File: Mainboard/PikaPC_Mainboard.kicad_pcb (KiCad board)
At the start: 2 copper layers, 190.5 x 147.3 mm, 87 parts, among them J1 Conn_02x08_Odd_Even, J10 Conn_01x08, J11 Conn_01x08, J12 Conn_01x08, J13 Conn_01x08, J14 Conn_01x08, J15 Conn_01x08, J16 Conn_01x08, J17 Conn_01x08, J18 Conn_01x10, J19 Conn_02x05_Odd_Even, J5 DIN41612_03x32_C_Split, J6 Mini-DIN-6, J7 Mini-DIN-6, J9 Conn_01x08, SW1 SW_Push_DPDT, SW2 SW_Push, U1 PPC403GA, U10 74LS07, U11 86C325, U12 GD75232N, U13 74LVC125, U14 MCP120-315GI/TO, U15 AS6C4008-55PCN, U16 AS6C4008-55PCN, U17 ATF1504, U18 T224162B, U19 T224162B, U2 SN74LVC245A, U20 T224162B, U21 T224162B, U22 SN74LVC245A, U23 SN74LVC245A, U3 SST39VF010, U4 SN74LVC245A, U5 SN74LVC245A, U6 SN74LVC245A, U7 8042 PS/2, U8 SN74LVC245A, U9 74LS04, Y1 25M, Y2 7M3728, Y3 14M31818

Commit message: VRAM control debugging
- correct clock edge for VLB ReadyIn
- minor tweaks for S3 ViRGE symbol
- add series resistors to VRAM control signals
- add strapping resistor to support Trio64V+
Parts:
- added RN10: 33R, Resistor_THT:R_Array_SIP10, F.Cu at (195.6, 27.9)
- added RN11: 33R, Resistor_THT:R_Array_SIP10, F.Cu at (205.7, 43.2)
- added RN12: 33R, Resistor_THT:R_Array_SIP10, F.Cu at (205.7, 71.1)
- added RN9: 10X-1-472LF, Resistor_THT:R_Array_SIP10, F.Cu at (195.6, 33.0)
- moved C24 52.3 mm to (149.9, 45.7), turned to 0 degrees
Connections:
- RN5 pad 2: unconnected-(RN5-R1-Pad2) -> /VID-SAUP2
- RN6 pad 7: unconnected-(RN6-R6-Pad7) -> /VMD24
- U11 pad 148: unconnected-(U11D-LCLK-Pad148) -> /VLCLK
- U11 pad 203: unconnected-(U11D-~{VREQ}-Pad203) -> /VEVIDEO
- U11 pad 204: unconnected-(U11D-~{CREQ}-Pad204) -> /~{VCREQ}
- U11 pad 205: unconnected-(U11D-SPCLK-Pad205) -> /VESYNC
- U11 pad 206: unconnected-(U11D-SPD-Pad206) -> /~{VBLANK}
- U18 pad 13: /~{VMWE} -> /~{VMWER}
- U18 pad 14: /~{VMRAS0} -> /~{VMRAS0R}
- U18 pad 27: /~{VMOE} -> /~{VMOER}
- U19 pad 13: /~{VMWE} -> /~{VMWER}
- U19 pad 14: /~{VMRAS0} -> /~{VMRAS0R}
- U19 pad 27: /~{VMOE} -> /~{VMOER}
- U20 pad 13: /~{VMWE} -> /~{VMWER}
- U20 pad 14: /~{VMRAS0} -> /~{VMRAS0R}
- U20 pad 27: /~{VMOE} -> /~{VMOER}
- U21 pad 13: /~{VMWE} -> /~{VMWER}
- U21 pad 14: /~{VMRAS0} -> /~{VMRAS0R}
- U21 pad 27: /~{VMOE} -> /~{VMOER}
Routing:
- net /~{VMRAS0}: track 37.9 -> 8.86 mm
- net /~{VMRAS0R}: track 0.00 -> 29.1 mm
- net /~{VMOER}: track 0.00 -> 29.1 mm
- net /~{VMOE}: track 37.7 -> 8.66 mm
- net unconnected-(U11D-SPCLK-Pad205): track 18.4 -> 0.00 mm
- net /VESYNC: track 0.00 -> 18.4 mm
- net /~{VMWE}: track 28.2 -> 11.4 mm
- net /~{VMWER}: track 0.00 -> 16.8 mm
- net unconnected-(U11D-~{CREQ}-Pad204): track 15.8 -> 0.00 mm
- net /~{VCREQ}: track 0.00 -> 15.8 mm
- net unconnected-(U11D-SPD-Pad206): track 13.1 -> 0.00 mm
- net /~{VBLANK}: track 0.00 -> 13.1 mm
- net unconnected-(U11D-~{VREQ}-Pad203): track 11.8 -> 0.00 mm
- net /VEVIDEO: track 0.00 -> 11.8 mm
- net unconnected-(U11D-LCLK-Pad148): track 10.6 -> 0.00 mm
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
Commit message: Add new bus to wire-wrap mainboard
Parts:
- removed C19, C20, C21, C22: 47p, Capacitor_THT:C_Disc_D3.0mm_W2.0mm_P2.50mm
- removed C23, C24: 100nF, Capacitor_THT:C_Disc_D3.0mm_W2.0mm_P2.50mm
- removed FB1, FB2, FB3: FerriteBead, Inductor_THT:L_Axial_L7.0mm_D3.3mm_P5.08mm_Vertical_Fastron_MICC
- removed J1: Conn_02x08_Odd_Even, Connector_PinHeader_2.54mm:PinHeader_2x08_P2.54mm_Vertical
- removed J6, J7: Mini-DIN-6, Connector_PinHeader_2.54mm:PinHeader_2x03_P2.54mm_Vertical
- removed R11, R6, R7: 75R, Resistor_THT:R_Axial_DIN0204_L3.6mm_D1.6mm_P2.54mm_Vertical
- removed R2: 220R, Resistor_THT:R_Axial_DIN0204_L3.6mm_D1.6mm_P2.54mm_Vertical
- removed R3: 470R, Resistor_THT:R_Axial_DIN0204_L3.6mm_D1.6mm_P2.54mm_Vertical
- removed RN10, RN11, RN12: 33R, Resistor_THT:R_Array_SIP10
- removed RN4, RN6, RN8: 9A103J, Resistor_THT:R_Array_SIP9
- removed RN7: 10X-1-472F, Resistor_THT:R_Array_SIP9
- removed RN9: 10X-1-472LF, Resistor_THT:R_Array_SIP10
- removed U11: 86C325, Package_QFP:PQFP-208_28x28mm_P0.5mm
- removed U17: ATF1504, Package_LCC:PLCC-44_THT-Socket
- removed U18, U19, U20, U21: T224162B, Package_SO:SOJ-44_10.16x28.575mm_P1.27mm
- removed U22, U23, U4, U5, U6, U8: SN74LVC245A, Package_DIP:DIP-20_W7.62mm_Socket
- removed U7: 8042 PS/2, Package_DIP:DIP-40_W15.24mm_Socket
- removed Y3: 14M31818, Oscillator:Oscillator_DIP-8
- added U101: SN74LVC245A, Package_DIP:DIP-20_W7.62mm_Socket, F.Cu at (104.1, 78.7)
- added U102: SN74LVC245A, Package_DIP:DIP-20_W7.62mm_Socket, F.Cu at (132.1, 78.7)
- added U103: SN74LVC245A, Package_DIP:DIP-20_W7.62mm_Socket, F.Cu at (104.1, 66.0)
- added U104: SN74LVC245A, Package_DIP:DIP-20_W7.62mm_Socket, F.Cu at (132.1, 66.0)
- added U105: SN74LVC245A, Package_DIP:DIP-20_W7.62mm_Socket, F.Cu at (132.1, 53.3)
- added U106: SN74LVC245A, Package_DIP:DIP-20_W7.62mm_Socket, F.Cu at (104.1, 53.3)
- added U107: SN74LVC245A, Package_DIP:DIP-20_W7.62mm_Socket, F.Cu at (104.1, 40.6)
- added U108: SN74LVC245A, Package_DIP:DIP-20_W7.62mm_Socket, F.Cu at (132.1, 40.6)
- added U109: 74LS244, Package_DIP:DIP-20_W7.62mm_Socket, F.Cu at (195.6, 78.7)
- added U110: 74LS244, Package_DIP:DIP-20_W7.62mm_Socket, F.Cu at (195.6, 66.0)
- added U111: 74LS244, Package_DIP:DIP-20_W7.62mm_Socket, F.Cu at (195.6, 53.3)
- added U112: 74LS244, Package_DIP:DIP-20_W7.62mm_Socket, F.Cu at (195.6, 40.6)
- U2: value SN74LVC245A -> ATF1508AS; footprint Package_DIP:DIP-20_W7.62mm_Socket -> Package_LCC:PLCC-84_THT-Socket
- moved RN5 163.7 mm to (-21.3, 68.1)
- moved U10 145.9 mm to (-25.5, 79.7)
- moved U9 120.7 mm to (-25.5, 68.0)
- moved J5 73.7 mm to (172.7, 15.2)
- moved U2 36.4 mm to (137.2, 63.5), turned to 90 degrees
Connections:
- J5 pad a1: unconnected-(J5A-Pin_a1-Pada1) -> GND
- J5 pad a10: unconnected-(J5A-Pin_a10-Pada10) -> /AD9
- J5 pad a11: unconnected-(J5A-Pin_a11-Pada11) -> /AD11
- J5 pad a12: unconnected-(J5A-Pin_a12-Pada12) -> /AD13
- J5 pad a13: unconnected-(J5A-Pin_a13-Pada13) -> /AD15
- J5 pad a14: unconnected-(J5A-Pin_a14-Pada14) -> /AD17
- J5 pad a15: unconnected-(J5A-Pin_a15-Pada15) -> /AD19
- J5 pad a16: unconnected-(J5A-Pin_a16-Pada16) -> /AD21
- J5 pad a17: unconnected-(J5A-Pin_a17-Pada17) -> /AD23
- J5 pad a18: unconnected-(J5A-Pin_a18-Pada18) -> /AD25
- J5 pad a19: unconnected-(J5A-Pin_a19-Pada19) -> /AD27
- J5 pad a2: unconnected-(J5A-Pin_a2-Pada2) -> +5V
- J5 pad a20: unconnected-(J5A-Pin_a20-Pada20) -> /AD29
- J5 pad a21: unconnected-(J5A-Pin_a21-Pada21) -> /AD31
- J5 pad a22: unconnected-(J5A-Pin_a22-Pada22) -> +3.3V
- J5 pad a23: unconnected-(J5A-Pin_a23-Pada23) -> +3.3V
- J5 pad a24: unconnected-(J5A-Pin_a24-Pada24) -> /~{Bus-BE1}
- J5 pad a25: unconnected-(J5A-Pin_a25-Pada25) -> /~{Bus-BE3}
- J5 pad a26: unconnected-(J5A-Pin_a26-Pada26) -> /~{Bus-BURST}
- J5 pad a27: unconnected-(J5A-Pin_a27-Pada27) -> /~{Bus-ACK}
- J5 pad a28: unconnected-(J5A-Pin_a28-Pada28) -> GND
- J5 pad a29: unconnected-(J5A-Pin_a29-Pada29) -> /Bus-Clk
- J5 pad a3: unconnected-(J5A-Pin_a3-Pada3) -> /~{Bus-IRQ0}
- J5 pad a30: unconnected-(J5A-Pin_a30-Pada30) -> +12V
- J5 pad a31: unconnected-(J5A-Pin_a31-Pada31) -> +5V
- J5 pad a32: unconnected-(J5A-Pin_a32-Pada32) -> GND
- J5 pad a4: unconnected-(J5A-Pin_a4-Pada4) -> /~{Bus-IRQ1}
- J5 pad a5: unconnected-(J5A-Pin_a5-Pada5) -> /~{Bus-IRQ2}
- J5 pad a6: unconnected-(J5A-Pin_a6-Pada6) -> /AD1
- J5 pad a7: unconnected-(J5A-Pin_a7-Pada7) -> /AD3
- J5 pad a8: unconnected-(J5A-Pin_a8-Pada8) -> /AD5
- J5 pad a9: unconnected-(J5A-Pin_a9-Pada9) -> /AD7
- J5 pad b1: unconnected-(J5B-Pin_b1-Padb1) -> GND
- J5 pad b10: unconnected-(J5B-Pin_b10-Padb10) -> GND
- J5 pad b11: unconnected-(J5B-Pin_b11-Padb11) -> GND
- J5 pad b12: unconnected-(J5B-Pin_b12-Padb12) -> GND
- J5 pad b13: unconnected-(J5B-Pin_b13-Padb13) -> GND
- J5 pad b14: unconnected-(J5B-Pin_b14-Padb14) -> GND
- J5 pad b15: unconnected-(J5B-Pin_b15-Padb15) -> GND
- J5 pad b16: unconnected-(J5B-Pin_b16-Padb16) -> GND
- J5 pad b17: unconnected-(J5B-Pin_b17-Padb17) -> GND
- J5 pad b18: unconnected-(J5B-Pin_b18-Padb18) -> GND
- J5 pad b19: unconnected-(J5B-Pin_b19-Padb19) -> GND
- J5 pad b2: unconnected-(J5B-Pin_b2-Padb2) -> +5V
- J5 pad b20: unconnected-(J5B-Pin_b20-Padb20) -> GND
- J5 pad b21: unconnected-(J5B-Pin_b21-Padb21) -> GND
- J5 pad b28: unconnected-(J5B-Pin_b28-Padb28) -> GND
- J5 pad b29: unconnected-(J5B-Pin_b29-Padb29) -> GND
- J5 pad b3: unconnected-(J5B-Pin_b3-Padb3) -> +5V
- J5 pad b30: unconnected-(J5B-Pin_b30-Padb30) -> GND
- J5 pad b31: unconnected-(J5B-Pin_b31-Padb31) -> +5V
- J5 pad b32: unconnected-(J5B-Pin_b32-Padb32) -> GND
- J5 pad b4: unconnected-(J5B-Pin_b4-Padb4) -> +5V
- J5 pad b5: unconnected-(J5B-Pin_b5-Padb5) -> +3.3V
- J5 pad b6: unconnected-(J5B-Pin_b6-Padb6) -> +3.3V
- J5 pad b7: unconnected-(J5B-Pin_b7-Padb7) -> GND
- J5 pad b8: unconnected-(J5B-Pin_b8-Padb8) -> GND
- J5 pad b9: unconnected-(J5B-Pin_b9-Padb9) -> GND
- J5 pad c1: unconnected-(J5C-Pin_c1-Padc1) -> GND
- J5 pad c10: unconnected-(J5C-Pin_c10-Padc10) -> /AD8
- J5 pad c11: unconnected-(J5C-Pin_c11-Padc11) -> /AD10
- J5 pad c12: unconnected-(J5C-Pin_c12-Padc12) -> /AD12
- J5 pad c13: unconnected-(J5C-Pin_c13-Padc13) -> /AD14
- J5 pad c14: unconnected-(J5C-Pin_c14-Padc14) -> /AD16
- J5 pad c15: unconnected-(J5C-Pin_c15-Padc15) -> /AD18
- J5 pad c16: unconnected-(J5C-Pin_c16-Padc16) -> /AD20
- J5 pad c17: unconnected-(J5C-Pin_c17-Padc17) -> /AD22
- J5 pad c18: unconnected-(J5C-Pin_c18-Padc18) -> /AD24
- J5 pad c19: unconnected-(J5C-Pin_c19-Padc19) -> /AD26
- J5 pad c2: unconnected-(J5C-Pin_c2-Padc2) -> +5V
- J5 pad c20: unconnected-(J5C-Pin_c20-Padc20) -> /AD28
- J5 pad c21: unconnected-(J5C-Pin_c21-Padc21) -> /AD30
- J5 pad c22: unconnected-(J5C-Pin_c22-Padc22) -> /~{Bus-REQ}
- J5 pad c23: unconnected-(J5C-Pin_c23-Padc23) -> /~{Bus-GNT}
- J5 pad c24: unconnected-(J5C-Pin_c24-Padc24) -> /~{Bus-BE0}
- J5 pad c25: unconnected-(J5C-Pin_c25-Padc25) -> /~{Bus-BE2}
- J5 pad c26: unconnected-(J5C-Pin_c26-Padc26) -> /~{Bus-BRACK}
- J5 pad c27: unconnected-(J5C-Pin_c27-Padc27) -> /~{Bus-Start}
- J5 pad c28: unconnected-(J5C-Pin_c28-Padc28) -> /~{Bus-BERR}
- J5 pad c29: unconnected-(J5C-Pin_c29-Padc29) -> GND
- J5 pad c3: unconnected-(J5C-Pin_c3-Padc3) -> /~{Bus-Reset}
- J5 pad c30: unconnected-(J5C-Pin_c30-Padc30) -> -12V
- J5 pad c31: unconnected-(J5C-Pin_c31-Padc31) -> +5V
- J5 pad c32: unconnected-(J5C-Pin_c32-Padc32) -> GND
- J5 pad c4: unconnected-(J5C-Pin_c4-Padc4) -> /~{Bus-IACK}
- J5 pad c5: unconnected-(J5C-Pin_c5-Padc5) -> /Bus-R/~{W}
- J5 pad c6: unconnected-(J5C-Pin_c6-Padc6) -> /AD0
- J5 pad c7: unconnected-(J5C-Pin_c7-Padc7) -> /AD2
- J5 pad c8: unconnected-(J5C-Pin_c8-Padc8) -> /AD4
- J5 pad c9: unconnected-(J5C-Pin_c9-Padc9) -> /AD6
- U10 pad 1: /~{MSDO} -> (no net)
- U10 pad 2: MDAT -> (no net)
- U10 pad 3: /~{MSCO} -> (no net)
- U10 pad 4: MCLK -> (no net)
- U10 pad 5: /~{KBCO} -> (no net)
- U10 pad 6: KCLK -> (no net)
- U10 pad 8: KDAT -> (no net)
- U10 pad 9: /~{KBDO} -> (no net)
- U2 pad 1: /R/~{W} -> /~{Reset}
- U2 pad 10: GND -> unconnected-(U2A-IO6-Pad10)
- U2 pad 11: /D23 -> unconnected-(U2A-IO5-Pad11)
- U2 pad 12: /D22 -> /R/~{W}
- U2 pad 13: /D21 -> +5V
- U2 pad 14: /D20 -> unconnected-(U2A-TDI/IO32-Pad14)
- U2 pad 15: /D19 -> /~{Bus-Start}
- U2 pad 16: /D18 -> /~{Bus-BE2}
- U2 pad 17: /D17 -> /~{Bus-BE3}
- U2 pad 18: /D16 -> /~{Bus-BE1}
- U2 pad 19: /~{PB32} -> GND
- U2 pad 2: /VD8 -> unconnected-(U2A-OE2-CGLK2-Pad2)
- U2 pad 20: +3.3V -> /~{Bus-ACK}
- U2 pad 3: /VD9 -> +5V
- U2 pad 4: /VD10 -> /~{Bus-IRQ2}
- U2 pad 5: /VD11 -> /~{Bus-IRQ1}
- U2 pad 6: /VD12 -> /~{Bus-IRQ0}
- U2 pad 7: /VD13 -> GND
- U2 pad 8: /VD14 -> unconnected-(U2A-IO11-Pad8)
- U2 pad 9: /VD15 -> unconnected-(U2A-IO8-Pad9)
- U9 pad 1: /MSDO -> (no net)
- U9 pad 2: /~{MSDO} -> (no net)
- U9 pad 3: /MSCO -> (no net)
- U9 pad 4: /~{MSCO} -> (no net)
- U9 pad 5: /KBCO -> (no net)
- U9 pad 6: /~{KBCO} -> (no net)
- U9 pad 8: /~{KBDO} -> (no net)
- U9 pad 9: /KBDO -> (no net)
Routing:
- net GND: track 645.7 -> 330.6 mm
- net +5V: track 318.4 -> 17.7 mm
- net (no net): track 67.2 -> 0.00 mm
- net /VMA7: track 66.2 -> 0.00 mm
- net /VMA5: track 43.2 -> 0.00 mm
- net /VMA4: track 42.3 -> 0.00 mm
- net /VMA0: track 40.4 -> 0.00 mm
- net /VMA2: track 37.3 -> 0.00 mm
- net /VMA8: track 30.6 -> 0.00 mm
- net /VMA1: track 30.5 -> 0.00 mm
- net /~{VMRAS0R}: track 29.1 -> 0.00 mm
- net /~{VMOER}: track 29.1 -> 0.00 mm
- net /VMA3: track 28.2 -> 0.00 mm
- net /VMA6: track 27.8 -> 0.00 mm
- net /VMD0: track 26.8 -> 0.00 mm
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
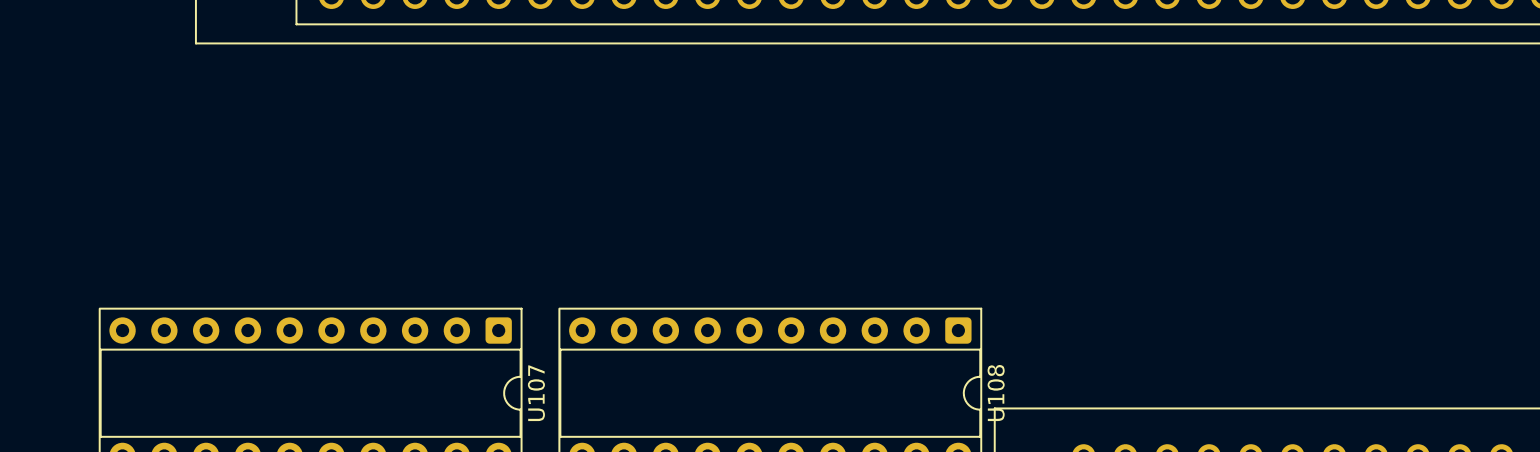
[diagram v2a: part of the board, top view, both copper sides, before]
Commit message: new bus control logic
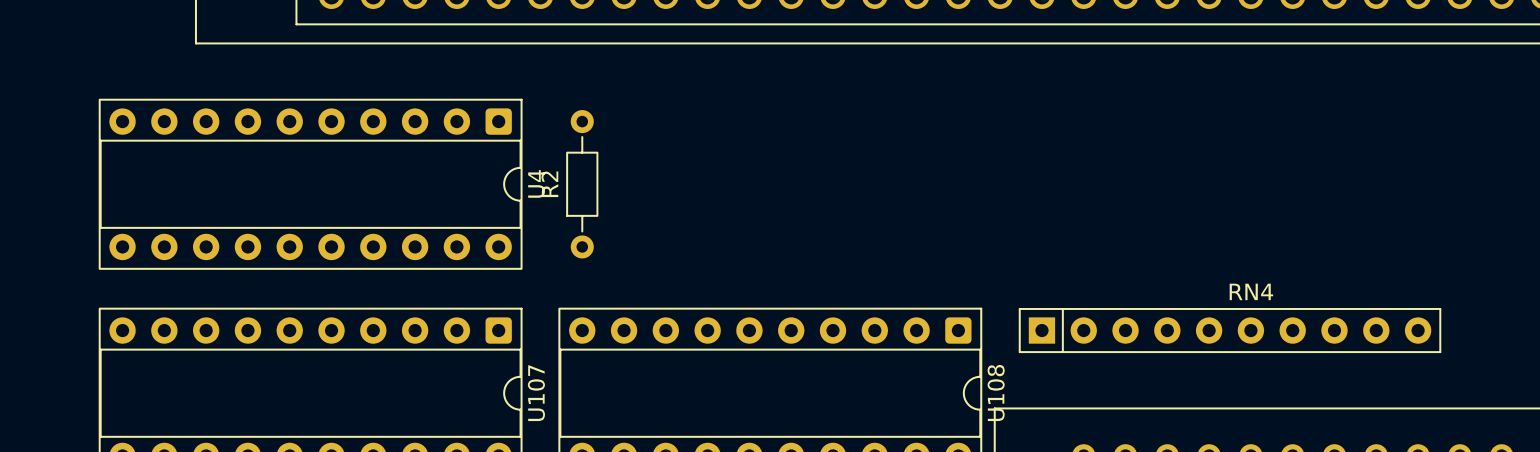
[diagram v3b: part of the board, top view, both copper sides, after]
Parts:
- added R2: 4k7, Resistor_THT:R_Axial_DIN0204_L3.6mm_D1.6mm_P7.62mm_Horizontal, F.Cu at (109.2, 35.6)
- added RN4: 10X-1-102LF, Resistor_THT:R_Array_SIP10, F.Cu at (137.2, 40.6)
- added U4: 74AHCT244, Package_DIP:DIP-20_W7.62mm_Socket, F.Cu at (104.1, 27.9)
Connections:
- RN3 pad 3: unconnected-(RN3-R2-Pad3) -> /INT0
- RN3 pad 4: unconnected-(RN3-R3-Pad4) -> /INT1
- RN3 pad 5: unconnected-(RN3-R4-Pad5) -> /INT2
- U13 pad 1: /~{VID-SRDY} -> unconnected-(U13-Pad1)
- U13 pad 3: /Ready -> unconnected-(U13-Pad3)

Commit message: SIMM72 card logic
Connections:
- U4 pad 17: unconnected-(U4-I3b-Pad17) -> /~{Reset}
- U4 pad 3: unconnected-(U4-O3b-Pad3) -> /~{Bus-Reset}
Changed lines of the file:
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@@
 	(net 266 "unconnected-(U4-I2b-Pad15)")
 	(net 267 "unconnected-(U4-O0b-Pad9)")
-	(net 268 "unconnected-(U4-O3b-Pad3)")
-	(net 269 "unconnected-(U4-I1a-Pad4)")
-	(net 270 "unconnected-(U4-O1a-Pad16)")
-	(net 271 "/~{WBE2}")
-	(net 272 "/A1{slash}~{WBE1}")
-	(net 273 "/~{WBE3}")
-	(net 274 "/A0{slash}~{WBE0}")
-	(net 275 "unconnected-(U13-Pad1)")
-	(net 276 "unconnected-(U13-Pad4)")
-	(net 277 "unconnected-(U13-Pad5)")
-	(net 278 "unconnected-(U13-Pad6)")
-	(net 279 "unconnected-(U4-I1b-Pad13)")
-	(net 280 "unconnected-(U4-O2a-Pad14)")
-	(net 281 "unconnected-(U4-I0b-Pad11)")
-	(net 282 "unconnected-(U4-O1b-Pad7)")
-	(net 283 "unconnected-(U4-O2b-Pad5)")
-	(net 284 "unconnected-(U4-I3b-Pad17)")
-	(net 285 "Net-(U4-OEb)")
-	(net 286 "unconnected-(U13-Pad3)")
+	(net 268 "/~{WBE2}")
+	(net 269 "/A1{slash}~{WBE1}")
+	(net 270 "/~{WBE3}")
+	(net 271 "/A0{slash}~{WBE0}")
+	(net 272 "unconnected-(U13-Pad1)")
+	(net 273 "unconnected-(U13-Pad4)")
+	(net 274 "unconnected-(U13-Pad5)")
+	(net 275 "unconnected-(U13-Pad6)")
+	(net 276 "unconnected-(U4-I1b-Pad13)")
+	(net 277 "unconnected-(U4-O2a-Pad14)")
+	(net 278 "unconnected-(U4-I0b-Pad11)")
+	(net 279 "unconnected-(U4-O1b-Pad7)")
+	(net 280 "unconnected-(U4-O2b-Pad5)")
+	(net 281 "Net-(U4-OEb)")
+	(net 282 "unconnected-(U13-Pad3)")
+	(net 283 "unconnected-(U4-I1a-Pad4)")
+	(net 284 "unconnected-(U4-O1a-Pad16)")
 	(footprint "Package_DIP:DIP-14_W7.62mm_Socket"
 		(layer "F.Cu")
@@
 			(layers "*.Cu" "*.Mask")
 			(remove_unused_layers no)
-			(net 272 "/A1{slash}~{WBE1}")
+			(net 269 "/A1{slash}~{WBE1}")
 			(pinfunction "A0")
 			(pintype "input")
@@
 			(layers "*.Cu" "*.Mask")
 			(remove_unused_layers no)
-			(net 271 "/~{WBE2}")
+			(net 268 "/~{WBE2}")
 			(pinfunction "WE#")
 			(pintype "input")
@@
 			(layers "*.Cu" "*.Mask")
 			(remove_unused_layers no)
-			(net 285 "Net-(U4-OEb)")
+			(net 281 "Net-(U4-OEb)")
 			(pintype "passive")
 		)
@@
 			(layers "F.Cu" "F.Mask" "F.Paste")
 			(roundrect_rratio 0.25)
-			(net 273 "/~{WBE3}")
+			(net 270 "/~{WBE3}")
 			(pinfunction "~{WBE0}/A4")
 			(pintype "tri_state")
@@
 			(layers "*.Cu" "F.Mask" "F.Paste")
 			(remove_unused_layers no)
-			(net 273 "/~{WBE3}")
+			(net 270 "/~{WBE3}")
 			(pinfunction "~{WBE0}/A4")
 			(pintype "tri_state")
@@
 			(layers "F.Cu" "F.Mask" "F.Paste")
 			(roundrect_rratio 0.25)
-			(net 271 "/~{WBE2}")
+			(net 268 "/~{WBE2}")
 			(pinfunction "~{WBE1}/A5")
 			(pintype "tri_state")
@@
 			(layers "*.Cu" "F.Mask" "F.Paste")
 			(remove_unused_layers no)
-			(net 271 "/~{WBE2}")
+			(net 268 "/~{WBE2}")
 			(pinfunction "~{WBE1}/A5")
 			(pintype "tri_state")
@@
 			(layers "F.Cu" "F.Mask" "F.Paste")
 			(roundrect_rratio 0.25)
-			(net 272 "/A1{slash}~{WBE1}")
+			(net 269 "/A1{slash}~{WBE1}")
 			(pinfunction "~{WBE2}/A30")
 			(pintype "tri_state")
@@
 			(layers "*.Cu" "F.Mask" "F.Paste")
 			(remove_unused_layers no)
-			(net 272 "/A1{slash}~{WBE1}")
+			(net 269 "/A1{slash}~{WBE1}")
 			(pinfunction "~{WBE2}/A30")
 			(pintype "tri_state")
@@
 			(layers "F.Cu" "F.Mask" "F.Paste")
 			(roundrect_rratio 0.25)
-			(net 274 "/A0{slash}~{WBE0}")
+			(net 271 "/A0{slash}~{WBE0}")
 			(pinfunction "~{WBE3}/A31")
 			(pintype "tri_state")
@@
 			(layers "*.Cu" "F.Mask" "F.Paste")
 			(remove_unused_layers no)
-			(net 274 "/A0{slash}~{WBE0}")
+			(net 271 "/A0{slash}~{WBE0}")
 			(pinfunction "~{WBE3}/A31")
 			(pintype "tri_state")
@@
 			(remove_unused_layers no)
 			(roundrect_rratio 0.15625)
-			(net 275 "unconnected-(U13-Pad1)")
+			(net 272 "unconnected-(U13-Pad1)")
 			(pintype "input")
 		)
@@
 			(layers "*.Cu" "*.Mask")
 			(remove_unused_layers no)
-			(net 286 "unconnected-(U13-Pad3)")
+			(net 282 "unconnected-(U13-Pad3)")
 			(pintype "tri_state")
 		)
@@
 			(layers "*.Cu" "*.Mask")
 			(remove_unused_layers no)
-			(net 276 "unconnected-(U13-Pad4)")
+			(net 273 "unconnected-(U13-Pad4)")
 			(pintype "input")
 		)
@@
 			(layers "*.Cu" "*.Mask")
 			(remove_unused_layers no)
-			(net 277 "unconnected-(U13-Pad5)")
+			(net 274 "unconnected-(U13-Pad5)")
 			(pintype "input")
 		)
@@
 			(layers "*.Cu" "*.Mask")
 			(remove_unused_layers no)
-			(net 278 "unconnected-(U13-Pad6)")
+			(net 275 "unconnected-(U13-Pad6)")
 			(pintype "tri_state")
 		)
@@
 			(layers "*.Cu" "*.Mask")
 			(remove_unused_layers no)
-			(net 268 "unconnected-(U4-O3b-Pad3)")
+			(net 195 "/~{Bus-Reset}")
 			(pinfunction "O3b")
 			(pintype "tri_state")
@@
 			(layers "*.Cu" "*.Mask")
 			(remove_unused_layers no)
-			(net 269 "unconnected-(U4-I1a-Pad4)")
+			(net 283 "unconnected-(U4-I1a-Pad4)")
 			(pinfunction "I1a")
 			(pintype "input")
@@
 			(layers "*.Cu" "*.Mask")
 			(remove_unused_layers no)
-			(net 283 "unconnected-(U4-O2b-Pad5)")
+			(net 280 "unconnected-(U4-O2b-Pad5)")
 			(pinfunction "O2b")
 			(pintype "tri_state")
@@
 			(layers "*.Cu" "*.Mask")
 			(remove_unused_layers no)
-			(net 282 "unconnected-(U4-O1b-Pad7)")
+			(net 279 "unconnected-(U4-O1b-Pad7)")
 			(pinfunction "O1b")
 			(pintype "tri_state")
@@
 			(layers "*.Cu" "*.Mask")
 			(remove_unused_layers no)
-			(net 281 "unconnected-(U4-I0b-Pad11)")
+			(net 278 "unconnected-(U4-I0b-Pad11)")
 			(pinfunction "I0b")
 			(pintype "input")
@@
 			(layers "*.Cu" "*.Mask")
 			(remove_unused_layers no)
-			(net 279 "unconnected-(U4-I1b-Pad13)")
+			(net 276 "unconnected-(U4-I1b-Pad13)")
 			(pinfunction "I1b")
 			(pintype "input")
@@
 			(layers "*.Cu" "*.Mask")
 			(remove_unused_layers no)
-			(net 280 "unconnected-(U4-O2a-Pad14)")
+			(net 277 "unconnected-(U4-O2a-Pad14)")
 			(pinfunction "O2a")
 			(pintype "tri_state")
@@
 			(layers "*.Cu" "*.Mask")
 			(remove_unused_layers no)
-			(net 270 "unconnected-(U4-O1a-Pad16)")
+			(net 284 "unconnected-(U4-O1a-Pad16)")
 			(pinfunction "O1a")
 			(pintype "tri_state")
@@
 			(layers "*.Cu" "*.Mask")
 			(remove_unused_layers no)
-			(net 284 "unconnected-(U4-I3b-Pad17)")
+			(net 75 "/~{Reset}")
 			(pinfunction "I3b")
 			(pintype "input")
@@
 			(layers "*.Cu" "*.Mask")
 			(remove_unused_layers no)
-			(net 285 "Net-(U4-OEb)")
+			(net 281 "Net-(U4-OEb)")
 			(pinfunction "OEb")
 			(pintype "input")
@@
 			(layers "*.Cu" "*.Mask")
 			(remove_unused_layers no)
-			(net 272 "/A1{slash}~{WBE1}")
+			(net 269 "/A1{slash}~{WBE1}")
 			(pinfunction "A0")
 			(pintype "input")
@@
 			(layers "*.Cu" "*.Mask")
 			(remove_unused_layers no)
-			(net 273 "/~{WBE3}")
+			(net 270 "/~{WBE3}")
 			(pinfunction "WE#")
 			(pintype "input")
@@
 			(layers "*.Cu" "*.Mask")
 			(remove_unused_layers no)
-			(net 273 "/~{WBE3}")
+			(net 270 "/~{WBE3}")
 			(pinfunction "IO56")
 			(pintype "bidirectional")
@@
 			(layers "*.Cu" "*.Mask")
 			(remove_unused_layers no)
-			(net 271 "/~{WBE2}")
+			(net 268 "/~{WBE2}")
 			(pinfunction "IO53")
 			(pintype "bidirectional")
@@
 			(layers "*.Cu" "*.Mask")
 			(remove_unused_layers no)
-			(net 272 "/A1{slash}~{WBE1}")
+			(net 269 "/A1{slash}~{WBE1}")
 			(pinfunction "IO51")
 			(pintype "bidirectional")
@@
 			(layers "*.Cu" "*.Mask")
 			(remove_unused_layers no)
-			(net 274 "/A0{slash}~{WBE0}")
+			(net 271 "/A0{slash}~{WBE0}")
 			(pinfunction "IO49")
 			(pintype "bidirectional")
@@
 			(layers "*.Cu" "*.Mask")
 			(remove_unused_layers no)
-			(net 272 "/A1{slash}~{WBE1}")
+			(net 269 "/A1{slash}~{WBE1}")
 			(pinfunction "A1")
 			(pintype "input")
@@
 			(layers "*.Cu" "*.Mask")
 			(remove_unused_layers no)
-			(net 274 "/A0{slash}~{WBE0}")
+			(net 271 "/A0{slash}~{WBE0}")
 			(pinfunction "A0")
 			(pintype "input")
@@
 		(width 0.254)
 		(layer "F.Cu")
-		(net 272)
+		(net 269)
 	)
 	(segment
@@
 		(width 0.254)
 		(layer "F.Cu")
-		(net 272)
+		(net 269)
 	)
 	(segment
@@
 		(width 0.254)
 		(layer "F.Cu")
-		(net 272)
+		(net 269)
 	)
 	(segment
@@
 		(width 0.254)
 		(layer "F.Cu")
-		(net 272)
+		(net 269)
 	)
 	(segment
@@
 		(width 0.254)
 		(layer "F.Cu")
-		(net 274)
+		(net 271)
 	)
 	(segment
@@
 		(width 0.254)
 		(layer "F.Cu")
-		(net 274)
+		(net 271)
 	)
 	(segment
@@
 		(width 0.254)
 		(layer "F.Cu")
-		(net 274)
+		(net 271)
 	)
 	(group ""

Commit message: fix low two expansion bus address bits
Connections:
- R2 pad 1: +5V -> GND
- U109 pad 2: GND -> /XA31
- U109 pad 4: GND -> /XA30
- U2 pad 33: unconnected-(U2A-IO64-Pad33) -> /XA30
- U2 pad 35: unconnected-(U2A-IO59-Pad35) -> /XA31
